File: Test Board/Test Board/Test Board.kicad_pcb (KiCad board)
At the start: 4 copper layers, 50 x 100 mm, 108 parts, among them J10 Conn_Coaxial_Power, J11 Conn_Coaxial_Power, J13 Conn_Coaxial_Power, J8 Screw_Terminal_01x03, J9 Conn_Coaxial_Power, Q4 SST113, SW10 SW_SPDT, SW7 SW_SPDT, SW8 SW_SPDT, SW9 SW_SPDT, U27 OPA189, U28 BUF634A, U29 OPA189, U30 OPA189, U31 OPA189, U32 OPA189, U33 OPA189, U34 INA849, U35 LM13700, U36 OPA189, U37 VCA810

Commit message: Removed LH circuit, added anti-windup test circuit, simplified voltage control mechanism
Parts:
- removed C62: 100p, Capacitor_SMD:C_0805_2012Metric
- removed C63, C64: 6p, Capacitor_SMD:C_0805_2012Metric
- removed C65, C66, C67, C68, C69, C70, C73, C74, C75, C76, C77, C78, C79, C80, C81, C82, C83, C84, C85, C86, C87, C88, C89, C90, C91, C92, C93, C94: 100nF, Capacitor_SMD:C_0805_2012Metric
- removed C71, C72: 6.8uF, Capacitor_SMD:C_0805_2012Metric
- removed D10, D11, D9: D, Package_TO_SOT_SMD:TSOT-23
- removed J10, J11, J13, J9: Conn_Coaxial_Power, Connector_Coaxial:SMA_Amphenol_901-143_Horizontal
- removed J8: Screw_Terminal_01x03, TerminalBlock_4Ucon:TerminalBlock_4Ucon_1x03_P3.50mm_Horizontal
- removed Q4: SST113, Package_TO_SOT_SMD:SOT-23
- removed R100, R101: 20k, Resistor_SMD:R_0805_2012Metric
- removed R102, R64, R65, R72, R75, R76, R77, R78, R79, R81, R99: 10k, Resistor_SMD:R_0805_2012Metric
- removed R103, R104, R86, R87, R88, R97: 0, Resistor_SMD:R_0805_2012Metric
- removed R66: 3.3k, Resistor_SMD:R_0805_2012Metric
- removed R67, R68, R70, R71, R73, R74, R82, R90: 1k, Resistor_SMD:R_0805_2012Metric
- removed R69, R95: 50, Resistor_SMD:R_0805_2012Metric
- removed R80: DNP, Resistor_SMD:R_0805_2012Metric
- removed R83: 10, Resistor_SMD:R_0805_2012Metric
- removed R84: 100, Resistor_SMD:R_0805_2012Metric
- removed R85: 400k, Resistor_SMD:R_0805_2012Metric
- removed R89, R92, R93: 30k, Resistor_SMD:R_0805_2012Metric
- removed R91: 13k, Resistor_SMD:R_0805_2012Metric
- removed R94: 5k, Resistor_SMD:R_0805_2012Metric
- removed R96: 25, Resistor_SMD:R_0805_2012Metric
- removed R98: 650k, Resistor_SMD:R_0805_2012Metric
- removed RV10: 100k, Custom_Footprints:Bourns Circular Pots
- removed RV8, RV9: 100k, Potentiometer_THT:Potentiometer_Bourns_3296W_Vertical
- removed SW10, SW7, SW8, SW9: SW_SPDT, Custom_Footprints:TDD DIP Switch
- removed TP10, TP9: TestPoint, TestPoint:TestPoint_Loop_D2.60mm_Drill1.6mm_Beaded
- removed U27, U29, U30, U31, U32, U33, U36: OPA189, Package_SO:SOIC-8_3.9x4.9mm_P1.27mm
- removed U28: BUF634A, Custom_Footprints:BUF634AIDDAR
- removed U34: INA849, Package_SO:SOIC-8_3.9x4.9mm_P1.27mm
- removed U35: LM13700, Package_SO:SOIC-16_3.9x9.9mm_P1.27mm
- removed U37: VCA810, Package_SO:SOIC-8_3.9x4.9mm_P1.27mm
- added C1: 100nF, Capacitor_SMD:C_0805_2012Metric, F.Cu at (86.3, 163.2)
- added C10: 100nF, Capacitor_SMD:C_0805_2012Metric, F.Cu at (143.0, 95.9)
- added C11: 100nF, Capacitor_SMD:C_0805_2012Metric, F.Cu at (143.0, 98.9)
- added C12: 100nF, Capacitor_SMD:C_0805_2012Metric, F.Cu at (143.0, 101.9)
- added C13: 100nF, Capacitor_SMD:C_0805_2012Metric, F.Cu at (147.4, 86.8)
- added C14: 100nF, Capacitor_SMD:C_0805_2012Metric, F.Cu at (147.4, 89.8)
- added C15: 100nF, Capacitor_SMD:C_0805_2012Metric, F.Cu at (147.4, 92.8)
- added C16: 100nF, Capacitor_SMD:C_0805_2012Metric, F.Cu at (147.4, 95.9)
- added C17: 100nF, Capacitor_SMD:C_0805_2012Metric, F.Cu at (147.4, 98.9)
- added C18: 100nF, Capacitor_SMD:C_0805_2012Metric, F.Cu at (231.6, 38.0)
- added C19: 100nF, Capacitor_SMD:C_0805_2012Metric, F.Cu at (231.6, 41.0)
- added C2: 100nF, Capacitor_SMD:C_0805_2012Metric, F.Cu at (86.3, 166.2)
- added C20: 100nF, Capacitor_SMD:C_0805_2012Metric, F.Cu at (230.2, 101.0)
- added C21: 100nF, Capacitor_SMD:C_0805_2012Metric, F.Cu at (230.2, 104.0)
- added C22: 100nF, Capacitor_SMD:C_0805_2012Metric, F.Cu at (236.1, 38.0)
- added C23: 100nF, Capacitor_SMD:C_0805_2012Metric, F.Cu at (236.1, 41.0)
- added C24: 100nF, Capacitor_SMD:C_0805_2012Metric, F.Cu at (236.1, 44.0)
- added C25: 100nF, Capacitor_SMD:C_0805_2012Metric, F.Cu at (236.1, 47.0)
- added C26: 100nF, Capacitor_SMD:C_0805_2012Metric, F.Cu at (245.1, 147.7)
- added C27: 100nF, Capacitor_SMD:C_0805_2012Metric, F.Cu at (245.1, 150.7)
- added C28: 6.8uF, Capacitor_SMD:C_0805_2012Metric, F.Cu at (245.1, 153.7)
- added C29: 6.8uF, Capacitor_SMD:C_0805_2012Metric, F.Cu at (245.1, 156.8)
- added C3: 100nF, Capacitor_SMD:C_0805_2012Metric, F.Cu at (73.1, 79.2)
- added C30: 10n, Capacitor_SMD:C_0805_2012Metric, F.Cu at (170.2, 152.0)
- added C31: 100p, Capacitor_SMD:C_0805_2012Metric, F.Cu at (170.2, 155.0)
- added C32: 100p, Capacitor_SMD:C_0805_2012Metric, F.Cu at (170.2, 158.0)
- added C33: 6p, Capacitor_SMD:C_0805_2012Metric, F.Cu at (170.2, 161.0)
- added C34: 6p, Capacitor_SMD:C_0805_2012Metric, F.Cu at (170.2, 164.0)
- added C4: 100nF, Capacitor_SMD:C_0805_2012Metric, F.Cu at (138.5, 95.9)
- added C5: 100nF, Capacitor_SMD:C_0805_2012Metric, F.Cu at (138.5, 98.9)
- added C6: 100nF, Capacitor_SMD:C_0805_2012Metric, F.Cu at (138.5, 101.9)
- added C7: 100nF, Capacitor_SMD:C_0805_2012Metric, F.Cu at (143.0, 86.8)
- added C8: 100nF, Capacitor_SMD:C_0805_2012Metric, F.Cu at (143.0, 89.8)
- added C9: 100nF, Capacitor_SMD:C_0805_2012Metric, F.Cu at (143.0, 92.8)
- added D1: D, Package_TO_SOT_SMD:TSOT-23, F.Cu at (245.3, 24.2)
- added D2: D, Package_TO_SOT_SMD:TSOT-23, F.Cu at (245.3, 28.8)
- added D3: D, Package_TO_SOT_SMD:TSOT-23, F.Cu at (156.5, 152.9)
- added D4: D, Package_TO_SOT_SMD:TSOT-23, F.Cu at (156.5, 157.6)
- added D5: D, Package_TO_SOT_SMD:TSOT-23, F.Cu at (156.5, 162.3)
- added J1: Screw_Terminal_01x03, TerminalBlock_4Ucon:TerminalBlock_4Ucon_1x03_P3.50mm_Horizontal, F.Cu at (57.0, 93.5)
- added J2: Conn_Coaxial_Power, Connector_Coaxial:SMA_Amphenol_901-143_Horizontal, F.Cu at (36.9, 84.2)
- added J3: Conn_Coaxial_Power, Connector_Coaxial:SMA_Amphenol_901-143_Horizontal, F.Cu at (46.6, 84.2)
- added J4: Conn_Coaxial_Power, Connector_Coaxial:SMA_Amphenol_901-143_Horizontal, F.Cu at (56.3, 84.2)
- added J5: Conn_Coaxial_Power, Connector_Coaxial:SMA_Amphenol_901-143_Horizontal, F.Cu at (114.3, 50.0)
- added Q1: SST113, Package_TO_SOT_SMD:SOT-23, F.Cu at (243.7, 90.3)
- added R1: 1k, Resistor_SMD:R_0805_2012Metric, F.Cu at (86.3, 181.2)
- added R10: 0, Resistor_SMD:R_0805_2012Metric, F.Cu at (81.9, 94.2)
- added R11: 50, Resistor_SMD:R_0805_2012Metric, F.Cu at (81.9, 97.2)
- added R12: 0, Resistor_SMD:R_0805_2012Metric, F.Cu at (81.9, 100.1)
- added R13: 0, Resistor_SMD:R_0805_2012Metric, F.Cu at (86.3, 91.3)
- added R14: 10k, Resistor_SMD:R_0805_2012Metric, F.Cu at (124.7, 41.8)
- added R15: 1k, Resistor_SMD:R_0805_2012Metric, F.Cu at (124.7, 44.7)
- added R16: DNP, Resistor_SMD:R_0805_2012Metric, F.Cu at (124.7, 47.6)
- added R17: 10k, Resistor_SMD:R_0805_2012Metric, F.Cu at (231.6, 23.2)
- added R18: 10k, Resistor_SMD:R_0805_2012Metric, F.Cu at (230.2, 83.2)
- added R19: 1k, Resistor_SMD:R_0805_2012Metric, F.Cu at (230.2, 86.1)
- added R2: 1k, Resistor_SMD:R_0805_2012Metric, F.Cu at (86.3, 184.2)
- added R20: 10k, Resistor_SMD:R_0805_2012Metric, F.Cu at (231.6, 32.0)
- added R23: 10k, Resistor_SMD:R_0805_2012Metric, F.Cu at (236.0, 26.1)
- added R24: 10k, Resistor_SMD:R_0805_2012Metric, F.Cu at (236.0, 29.1)
- added R25: 50, Resistor_SMD:R_0805_2012Metric, F.Cu at (240.5, 141.8)
- added R26: 25, Resistor_SMD:R_0805_2012Metric, F.Cu at (240.5, 144.7)
- added R27: 20k, Resistor_SMD:R_0805_2012Metric, F.Cu at (244.9, 132.9)
- added R28: 10k, Resistor_SMD:R_0805_2012Metric, F.Cu at (244.9, 135.9)
- added R29: 10k, Resistor_SMD:R_0805_2012Metric, F.Cu at (244.9, 138.8)
- added R3: 1k, Resistor_SMD:R_0805_2012Metric, F.Cu at (86.3, 187.1)
- added R30: 20k, Resistor_SMD:R_0805_2012Metric, F.Cu at (244.9, 141.8)
- added R31: 10k, Resistor_SMD:R_0805_2012Metric, F.Cu at (161.4, 152.0)
- added R32: 10k, Resistor_SMD:R_0805_2012Metric, F.Cu at (161.4, 154.9)
- added R33: 10k, Resistor_SMD:R_0805_2012Metric, F.Cu at (161.4, 157.9)
- added R34: 3.3k, Resistor_SMD:R_0805_2012Metric, F.Cu at (161.4, 160.8)
- added R35: 10k, Resistor_SMD:R_0805_2012Metric, F.Cu at (161.4, 163.8)
- added R36: 100k, Resistor_SMD:R_0805_2012Metric, F.Cu at (161.4, 166.7)
- added R37: 1k, Resistor_SMD:R_0805_2012Metric, F.Cu at (165.8, 152.0)
- added R38: 100k, Resistor_SMD:R_0805_2012Metric, F.Cu at (165.8, 154.9)
- added R39: 1k, Resistor_SMD:R_0805_2012Metric, F.Cu at (165.8, 157.9)
- added R4: 1k, Resistor_SMD:R_0805_2012Metric, F.Cu at (86.3, 190.1)
- added R40: 10k, Resistor_SMD:R_0805_2012Metric, F.Cu at (165.8, 160.8)
- added R41: 1k, Resistor_SMD:R_0805_2012Metric, F.Cu at (165.8, 163.8)
- added R5: 10k, Resistor_SMD:R_0805_2012Metric, F.Cu at (90.7, 181.2)
- added R6: 10k, Resistor_SMD:R_0805_2012Metric, F.Cu at (90.7, 184.2)
- added R7: 0, Resistor_SMD:R_0805_2012Metric, F.Cu at (77.5, 97.2)
- added R8: 0, Resistor_SMD:R_0805_2012Metric, F.Cu at (77.5, 100.1)
- added R9: 0, Resistor_SMD:R_0805_2012Metric, F.Cu at (81.9, 91.3)
- added RV1: 100k, Potentiometer_THT:Potentiometer_Bourns_3296W_Vertical, F.Cu at (93.8, 141.5)
- added RV2: 100k, Potentiometer_THT:Potentiometer_Bourns_3296W_Vertical, F.Cu at (93.8, 147.9)
- added RV3: 10k, Custom_Footprints:Bourns Circular Pots, F.Cu at (44.3, 60.1)
- added RV4: 100k, Potentiometer_THT:Potentiometer_Bourns_3296W_Vertical, F.Cu at (167.2, 171.4)
- added RV5: 100k, Potentiometer_THT:Potentiometer_Bourns_3296W_Vertical, F.Cu at (167.2, 177.8)
- added SW1: SW_SPDT, Custom_Footprints:TDD DIP Switch, F.Cu at (48.0, 182.5)
- added SW2: SW_SPDT, Custom_Footprints:TDD DIP Switch, F.Cu at (53.5, 182.5)
- added SW3: SW_SPDT, Custom_Footprints:TDD DIP Switch, F.Cu at (58.9, 182.5)
- added SW4: SW_SPDT, Custom_Footprints:TDD DIP Switch, F.Cu at (64.3, 182.5)
- added TP1: TestPoint, TestPoint:TestPoint_Loop_D2.60mm_Drill1.6mm_Beaded, F.Cu at (245.2, 39.0)
- added TP2: TestPoint, TestPoint:TestPoint_Loop_D2.60mm_Drill1.6mm_Beaded, F.Cu at (245.2, 44.0)
- added U1: INA849, Package_SO:SOIC-8_3.9x4.9mm_P1.27mm, F.Cu at (125.0, 30.3)
- added U10: BUF634A, Custom_Footprints:BUF634AIDDAR, F.Cu at (164.0, 184.3)
- added U11: OPA189, Package_SO:SOIC-8_3.9x4.9mm_P1.27mm, F.Cu at (149.6, 173.6)
- added U12: OPA189, Package_SO:SOIC-8_3.9x4.9mm_P1.27mm, F.Cu at (149.6, 180.2)
- added U13: OPA189, Package_SO:SOIC-8_3.9x4.9mm_P1.27mm, F.Cu at (149.6, 186.8)
- added U2: OPA189, Package_SO:SOIC-8_3.9x4.9mm_P1.27mm, F.Cu at (225.2, 25.1)
- added U3: OPA189, Package_SO:SOIC-8_3.9x4.9mm_P1.27mm, F.Cu at (223.8, 88.7)
- added U4: OPA189, Package_SO:SOIC-8_3.9x4.9mm_P1.27mm, F.Cu at (225.2, 38.3)
- added U5: OPA189, Package_SO:SOIC-8_3.9x4.9mm_P1.27mm, F.Cu at (225.2, 44.8)
- added U6: VCA810, Package_SO:SOIC-8_3.9x4.9mm_P1.27mm, F.Cu at (236.8, 152.2)
- added U7: OPA189, Package_SO:SOIC-8_3.9x4.9mm_P1.27mm, F.Cu at (149.6, 153.8)
- added U8: OPA189, Package_SO:SOIC-8_3.9x4.9mm_P1.27mm, F.Cu at (149.6, 160.4)
- added U9: OPA189, Package_SO:SOIC-8_3.9x4.9mm_P1.27mm, F.Cu at (149.6, 167.0)
- R22: value 1k -> 100k
- moved R21 330.7 mm to (231.6, 35.0)
- moved R22 318.2 mm to (234.6, 80.2)
- moved D8 238.9 mm to (156.5, 176.2), turned to 0 degrees
- moved D7 238.2 mm to (156.5, 171.6), turned to 0 degrees
- moved D6 234.0 mm to (156.5, 166.9), turned to 0 degrees
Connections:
- D7 pad 2: Net-(D6-K) -> Net-(D7-A)
- D8 pad 1: Net-(D8-K) -> Net-(D7-A)
- D8 pad 2: Net-(D8-A) -> Net-(D6-K)
- R21 pad 1: Net-(J13-In) -> V_control
- R22 pad 1: GND -> Net-(U3--)
- R22 pad 2: Net-(J13-In) -> TEST_OUTPUT
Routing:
- net TEST_INPUT: track 165.2 -> 0.00 mm, vias 3 -> 0
- net TEST_OUTPUT: track 146.1 -> 0.00 mm, vias 2 -> 0
- net GND: track 100.9 -> 0.00 mm, vias 23 -> 0
- net POT_2_TEST: track 100.3 -> 0.00 mm, vias 5 -> 0
- net POT_3_TEST: track 87.3 -> 0.00 mm, vias 5 -> 0
- net POT_1_TEST: track 79.9 -> 0.00 mm, vias 5 -> 0
- net -15V_TEST: track 41.8 -> 0.00 mm, vias 15 -> 0
- net +15V_TEST: track 38.4 -> 0.00 mm, vias 13 -> 0
- net Net-(D7-K): track 34.0 -> 0.00 mm
- net Net-(U4--): track 24.1 -> 0.00 mm
- net Net-(D10-A): track 13.5 -> 0.00 mm
- net Net-(D11-K): track 13.4 -> 0.00 mm
- net Net-(J13-In): track 11.7 -> 0.00 mm
- net Net-(D6-K): track 11.1 -> 0.00 mm
- net Net-(D5-K): track 11.0 -> 0.00 mm
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- removed copper zone on In2.Cu, net +15V_TEST
- removed copper zone on B.Cu, net -15V_TEST
- removed copper zone on F.Cu, net GND
- removed copper zone on In1.Cu, net GND
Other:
- board outline removed
- board text removed: "Clamp Test"
- board text removed: "Exp(Log+Pot)"
- board text removed: "JFET+OpAmp"
- board text removed: "LM13700"
- board text removed: "VCA"

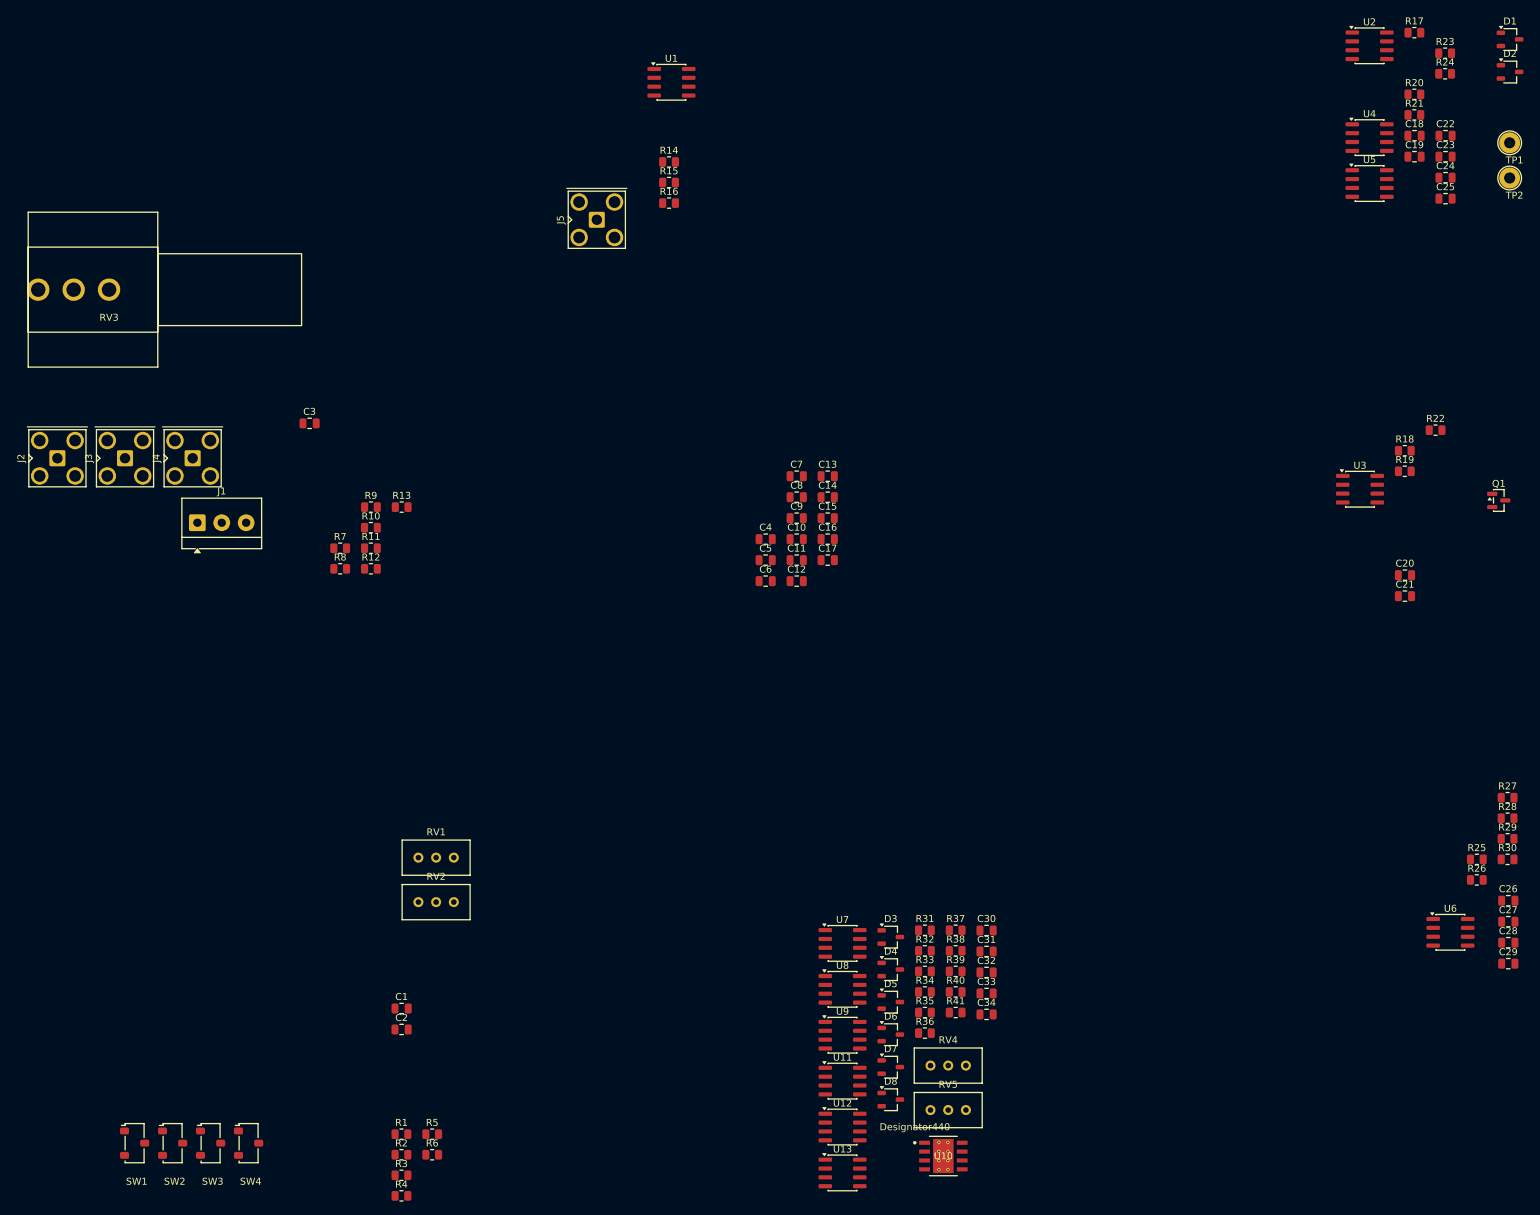
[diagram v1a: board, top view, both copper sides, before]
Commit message: First pass at routing Test Board, TODO: Find and Double check Part numbers
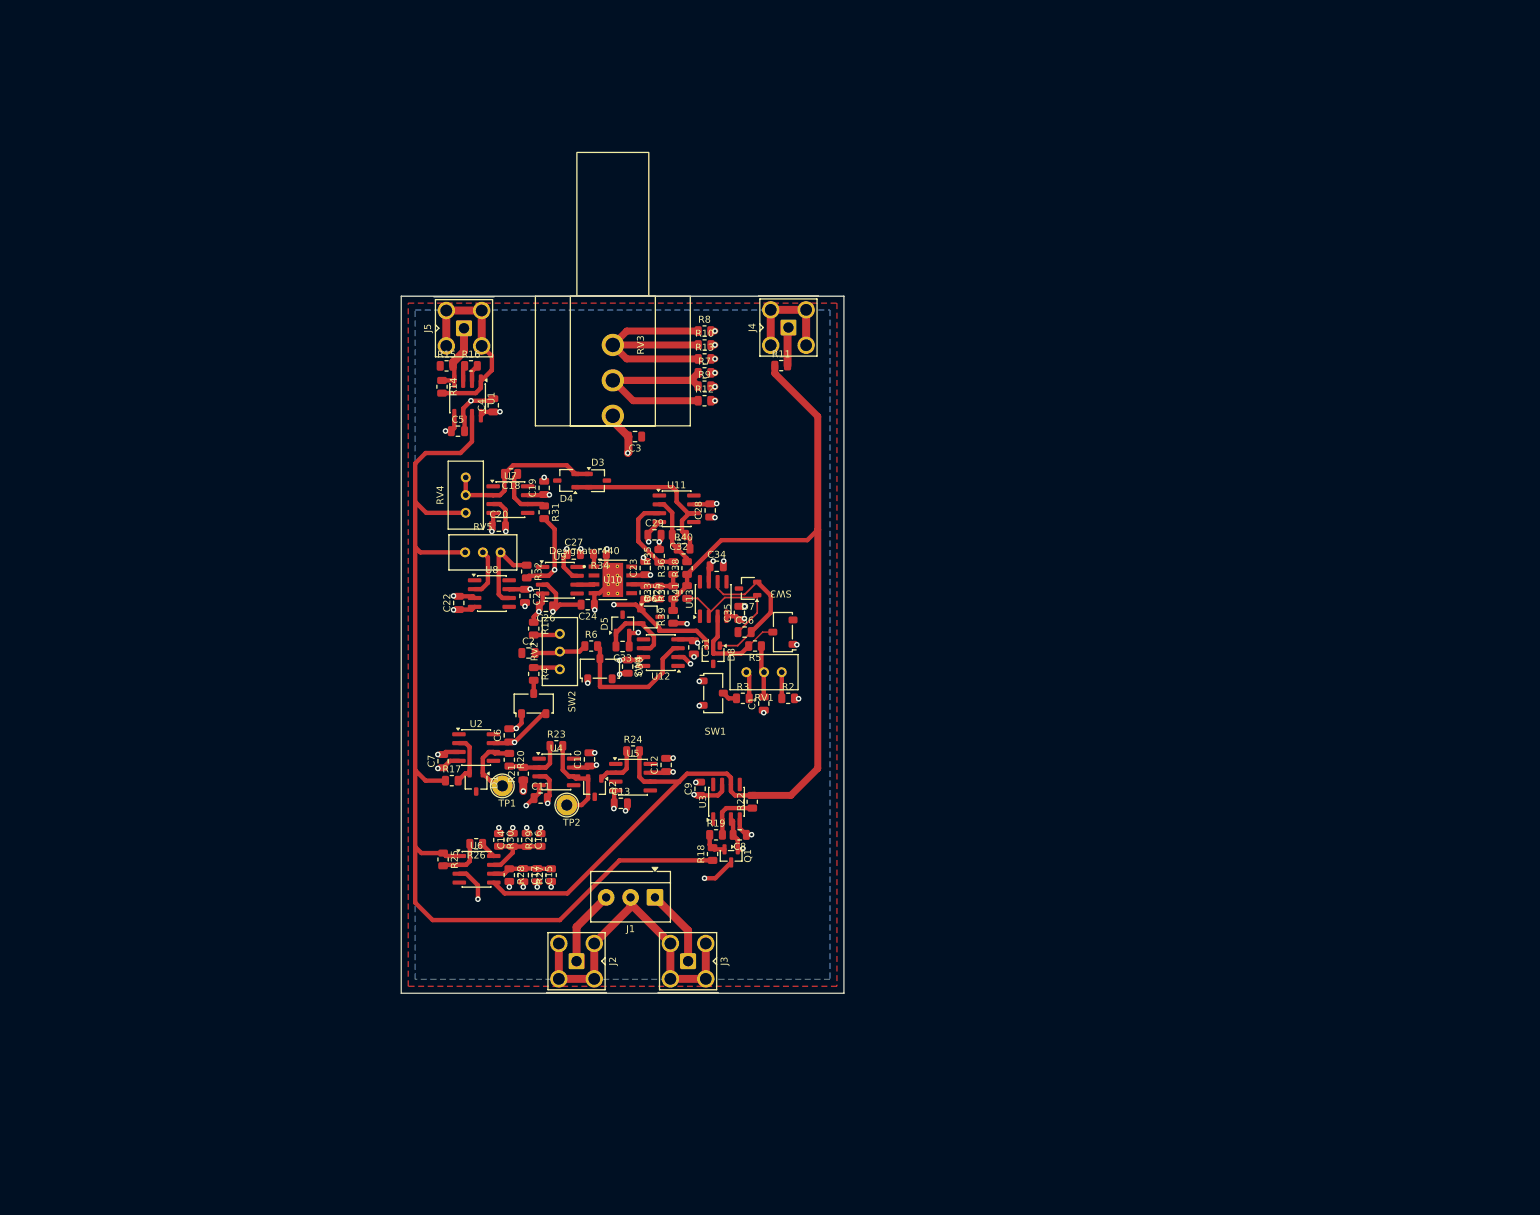
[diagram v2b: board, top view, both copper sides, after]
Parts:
- removed the C19 at (231.6, 41.0)
- added C18: 10n, Capacitor_SMD:C_0805_2012Metric, F.Cu at (102.0, 86.5)
- added C35: 100nF, Capacitor_SMD:C_0805_2012Metric, F.Cu at (134.8, 106.4)
- added C36: 6p, Capacitor_SMD:C_0805_2012Metric, F.Cu at (135.5, 109.2)
- C16, C17: value 100nF -> 6.8uF
- C25: value 100nF -> 100p
- C28, C29: value 6.8uF -> 100nF
- C30: value 10n -> 100nF
- C31: value 100p -> 100nF
- C34: value 6p -> 100nF
- moved D1 182.6 mm to (97.0, 130.8), turned to -90 degrees
- moved R17 174.9 mm to (93.5, 130.5)
- moved TP1 171.4 mm to (100.8, 131.2)
- moved D2 166.7 mm to (114.0, 131.5), turned to -90 degrees
- moved U2 163.0 mm to (97.0, 125.8)
- moved TP2 162.4 mm to (110.0, 134.0)
- moved R23 161.6 mm to (108.5, 125.5)
- moved R20 161.1 mm to (101.8, 127.5), turned to -90 degrees
- moved R21 159.0 mm to (103.8, 129.5), turned to 90 degrees
- moved C22 156.6 mm to (94.5, 105.0), turned to 90 degrees
- moved C6 155.8 mm to (101.8, 124.0), turned to 90 degrees
- moved R24 151.7 mm to (119.5, 126.2)
- moved R25 148.3 mm to (92.2, 141.8), turned to -90 degrees
- moved U4 147.9 mm to (108.5, 129.2)
- moved R30 144.7 mm to (100.2, 139.0), turned to -90 degrees
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- renumbered C6 to C19, C18 to C6
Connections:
- C11 pad 1: GND -> -15V
- C11 pad 2: -15V -> GND
- C13 pad 1: GND -> -15V
- C13 pad 2: -15V -> GND
- C14 pad 1: +15V -> Net-(U6-V-)
- C15 pad 1: GND -> Net-(U6-V+)
- C15 pad 2: -15V -> GND
- C16 pad 1: +15V -> GND
- C16 pad 2: GND -> Net-(U6-V-)
- C17 pad 1: GND -> Net-(U6-V+)
- C17 pad 2: -15V -> GND
- C22 pad 1: +15V -> -15V
- C23 pad 1: -15V -> +15V
- C24 pad 1: +15V -> -15V
- C25 pad 1: -15V -> Net-(U10-OUT)
- C25 pad 2: GND -> Net-(D6-K)
- C26 pad 1: Net-(U6-V-) -> GND
- C26 pad 2: GND -> -15V
- C27 pad 1: Net-(U6-V+) -> +15V
- C28 pad 2: Net-(U6-V-) -> +15V
- C29 pad 1: Net-(U6-V+) -> -15V
- C30 pad 1: Net-(C30-Pad1) -> +15V
- C30 pad 2: Net-(D3-K) -> GND
- C31 pad 1: Net-(U10-OUT) -> -15V
- C31 pad 2: Net-(D6-K) -> GND
- C34 pad 1: Net-(D7-K) -> +15V
- C34 pad 2: Net-(D7-A) -> GND
- C5 pad 1: GND -> -15V
- C5 pad 2: -15V -> GND
- C7 pad 1: GND -> -15V
- C7 pad 2: -15V -> GND
- C8 pad 1: +15V -> -15V
- C9 pad 1: GND -> +15V
- C9 pad 2: -15V -> GND
- R31 pad 1: Net-(C30-Pad1) -> Net-(C18-Pad1)
- U7 pad 6: Net-(C30-Pad1) -> Net-(C18-Pad1)
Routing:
- net TEST_OUTPUT: track 0.00 -> 155.8 mm
- net TEST_INPUT: track 0.00 -> 150.7 mm
- net GND: track 0.00 -> 134.0 mm, vias 0 -> 34
- net V_control: track 0.00 -> 127.9 mm, vias 0 -> 4
- net +15V: track 0.00 -> 62.3 mm, vias 0 -> 16
- net -15V: track 0.00 -> 61.1 mm, vias 0 -> 17
- net Net-(D6-K): track 0.00 -> 43.2 mm, vias 0 -> 2
- net Net-(R12-Pad1): track 0.00 -> 38.7 mm
- net Net-(R10-Pad1): track 0.00 -> 38.4 mm
- net Net-(J5-Ext): track 0.00 -> 28.4 mm
- net Net-(D3-A): track 0.00 -> 26.1 mm
- net Net-(D3-K): track 0.00 -> 23.9 mm
- net Net-(D7-A): track 0.00 -> 22.2 mm
- net V_CLAMP_N: track 0.00 -> 20.6 mm
- net Net-(D5-A): track 0.00 -> 20.2 mm, vias 0 -> 3
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- added copper zone on In2.Cu, net +15V
- added copper zone on B.Cu, net -15V
- added copper zone on F.Cu, net GND
- added copper zone on In1.Cu, net GND
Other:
- board outline added: 63.5 x 100 mm
